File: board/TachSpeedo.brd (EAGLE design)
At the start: 37.4 x 37.8 mm, 13 parts, among them J1 1-770969-0, P1 M-1X04-SIP-100-32, P2 M-1X03-SIP-100-32, U1 D24V5FX, U2 LPC810M, U3 MC33152, U4 MAX3483

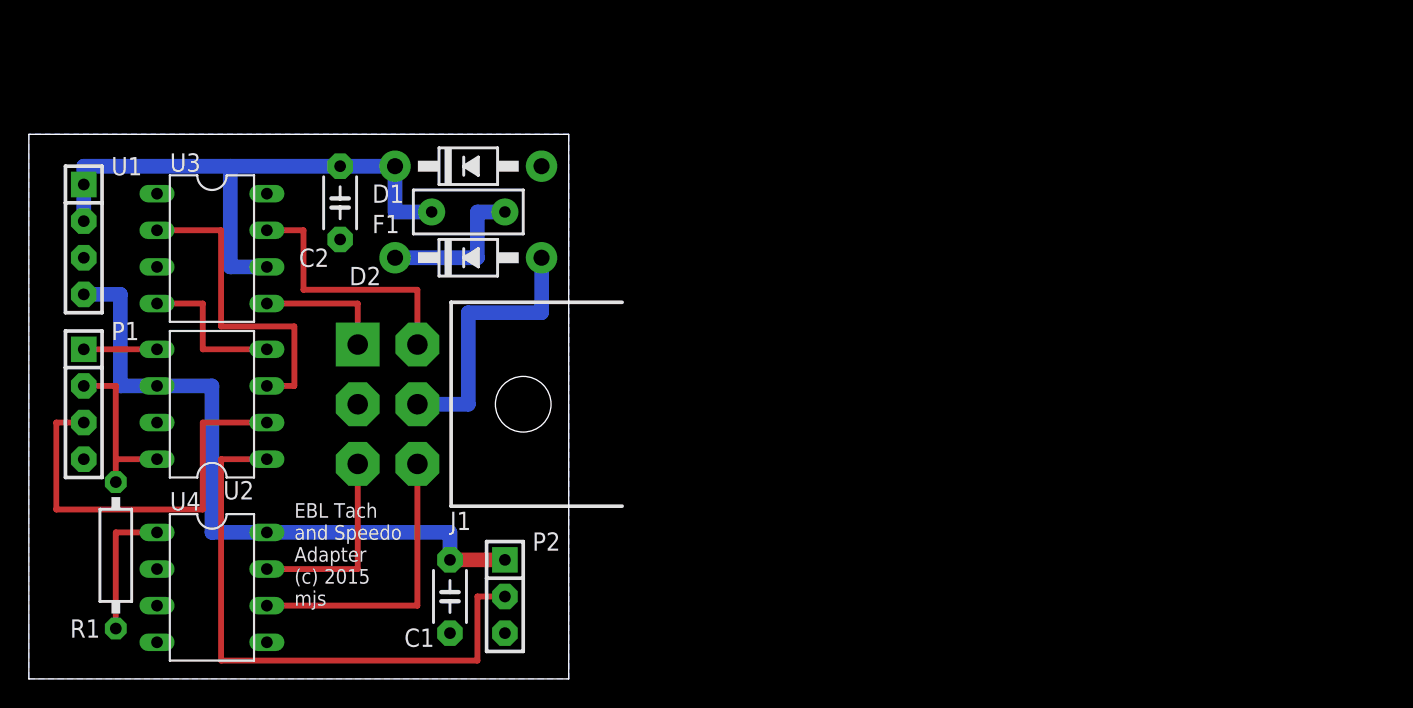
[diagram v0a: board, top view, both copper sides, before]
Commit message: Update in anticipation of the r3 board.
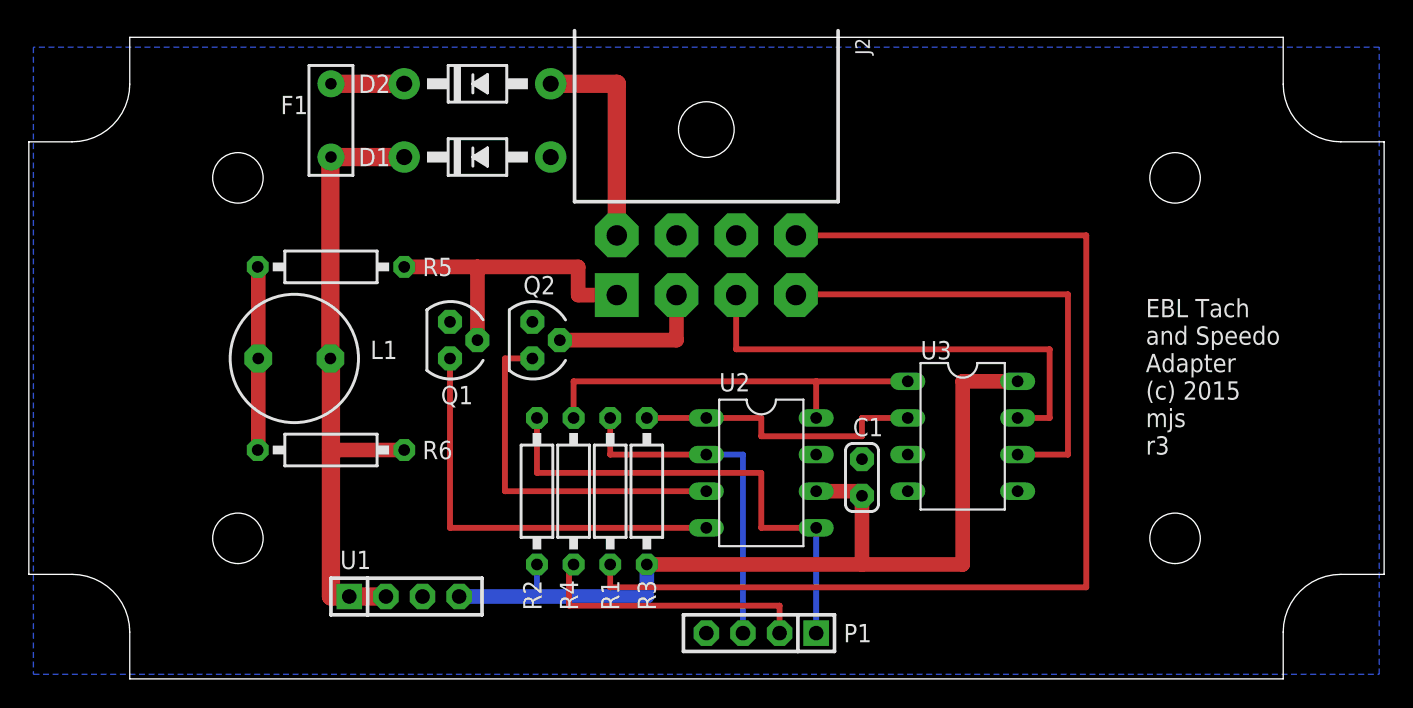
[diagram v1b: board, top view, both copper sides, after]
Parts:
- removed C2: 22u, custom:C050-024X044
- removed J1: 1-770969-0, custom:1-770969-0
- removed P2: M-1X03-SIP-100-32, custom:SIP-100-03-32
- removed U4: MAX3483, custom:DIL08
- added BOX1: HAMMOND-BOX-1591XXA, custom:1591XXA
- added J2: 1-770970-0, custom:1-770970-0
- added L1: RL622-683K-RC, custom:RL622
- added Q1, Q2: TND027MP, custom:TO-92
- added R2, R3, R4: 1K05, custom:0207/10
- added R5: 470R, custom:0207/10
- added R6: 1k5, custom:0207/10
- C1: value 22u -> 0u1; device custom:C050-024X044 -> custom:C025-024X044
- P1: value M-1X04-SIP-100-32 -> M-1X04-SIP-100-40; device custom:SIP-100-04-32 -> custom:SIP-100-04-40
- R1: value 1K0 -> 62R
- U1: value D24V5FX -> D24V5FXV; device custom:SIP-100-04-32 -> custom:SIP-100-04-40
- U3: value MC33152 -> MAX3483
- moved U3 53.7 mm to (64.8, 16.8)
- moved P1 49.6 mm to (50.8, 3.17), turned to 180 degrees
- moved U2 38.4 mm to (50.8, 14.3), turned to 270 degrees
- moved R1 34.6 mm to (40.3, 13.0), turned to 90 degrees
- moved U1 33.3 mm to (26.0, 5.71), turned to 0 degrees
- moved C1 29.7 mm to (57.8, 14.0), turned to 90 degrees
- moved D2 12.1 mm to (31.1, 41.3)
- moved F1 11.4 mm to (21.0, 38.7), turned to 270 degrees
- moved D1 0.90 mm to (31.1, 36.2)
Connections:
- removed net DRV0: U2.3, U3.2
- removed net DRV1: U2.4, U3.4
- removed net N$1: C2.1, D1.C, F1.P$2, U1.1, U1.2, U3.6
- removed net NEOPIXEL: P2.2, U2.1
- removed net OUT0: J1.4, U3.7
- removed net OUT1: J1.1, U3.5
- removed net TXD: P1.3, U2.2
- new net !RXEN: R3.1, U2.1, U3.2
- new net +12_FUSED: D1.C, F1.P$2, L1.2, R6.1, U1.1, U1.2
- new net DRV_SPEEDO: Q2.3, U2.3
- new net DRV_TACH: Q1.3, U2.4
- new net N$4: J2.8, R1.1
- new net N$6: L1.1, R5.1, R6.2
- new net OUT_SPEEDO: J2.2, Q2.2
- new net OUT_TACH: J2.1, Q1.2, R5.2
- new net TXD/CEL: P1.3, R1.2, U2.2
- net !PGM: now also R2.1
- net +12V: now also J2.5; no longer J1.5
- net +3V3: now also R2.2, R3.2, U3.8; no longer P2.1, U4.8
- net GND: now also J2.6, J2.7, Q1.1, Q2.1, U3.4, U3.5; no longer C2.2, J1.2, P2.3, U4.2, U4.3, U4.5
- net N$3: now also P1.2, R4.1; no longer R1.2, U4.1
- net RX+: now also J2.4, U3.6; no longer J1.6, U4.6
- net RX-: now also J2.3, U3.7; no longer J1.3, U4.7
- net RXD: now also R4.2, U3.1; no longer P1.2, R1.1
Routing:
- net N$4: track 0.00 -> 79.2 mm
- net +12_FUSED: track 0.00 -> 44.5 mm
- net NEOPIXEL: track 41.3 -> 0.00 mm
- net N$1: track 40.6 -> 0.00 mm
- net DRV_TACH: track 0.00 -> 29.5 mm
- net !PGM: track 5.08 -> 34.3 mm
- net TXD: track 28.6 -> 0.00 mm
- net DRV_SPEEDO: track 0.00 -> 25.1 mm
- net TXD/CEL: track 0.00 -> 24.1 mm
- net DRV0: track 22.2 -> 0.00 mm
- net OUT_TACH: track 0.00 -> 21.8 mm
- net !RXEN: track 0.00 -> 20.6 mm
- net RX-: track 13.6 -> 32.5 mm
- net OUT0: track 18.4 -> 0.00 mm
- net RXD: track 11.7 -> 28.3 mm
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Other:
- board size 37.4 x 37.8 mm -> 94 x 44.5 mm
- board text added: "EBL Tach and Speedo Adapter (c) 2015 mjs r3"
- board text removed: "EBL Tach and Speedo Adapter (c) 2015 mjs"
